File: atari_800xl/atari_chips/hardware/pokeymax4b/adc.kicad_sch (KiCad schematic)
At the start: 5 parts

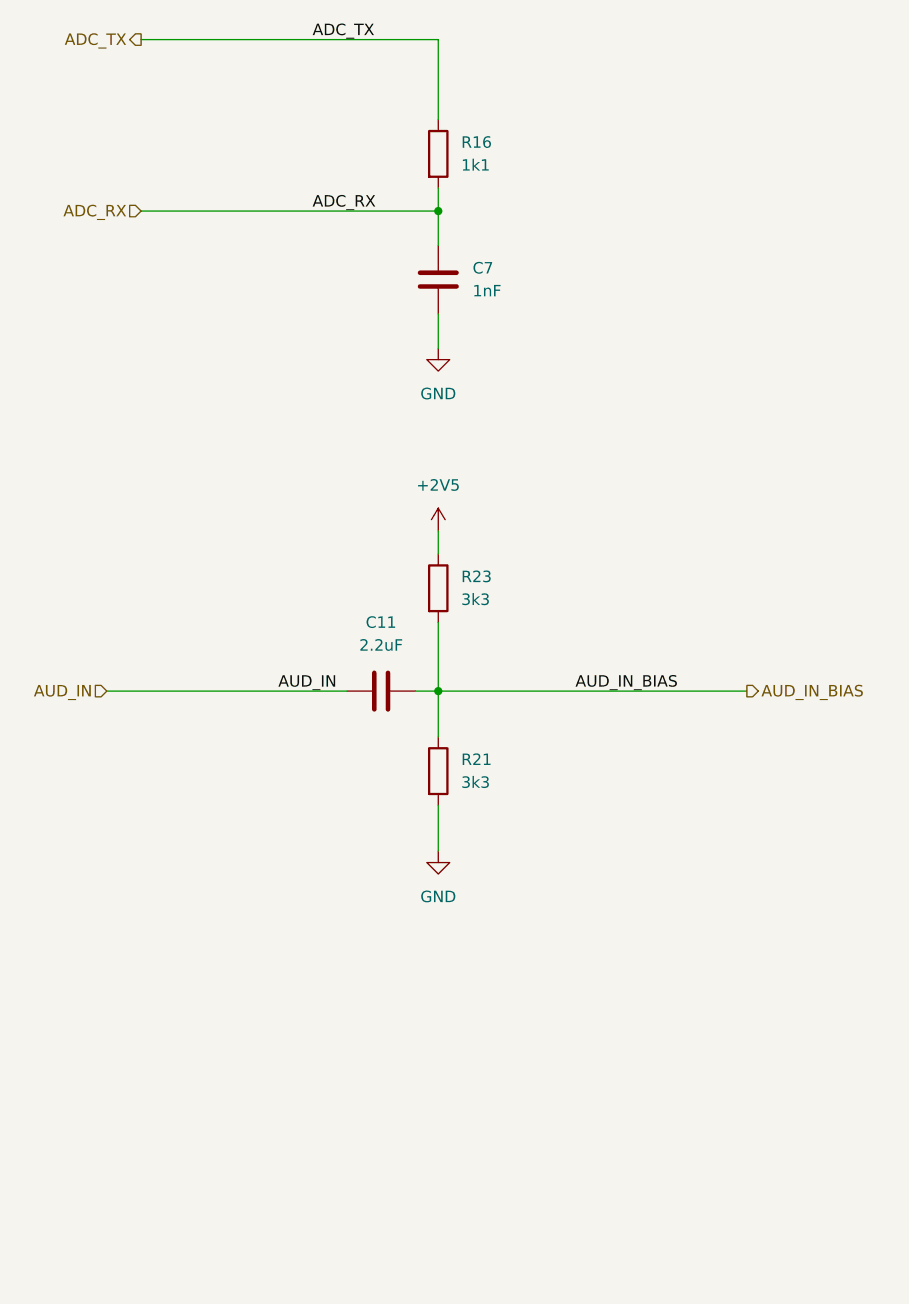
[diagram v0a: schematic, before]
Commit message: After testing 4b first run, there are a few issues. Updated to 4b2 with: Corrected L/R output. ADC bias improvement. ADC preamp out/in- corrected. Moved silkscreen name!
git-svn-id: svn+ssh://192.168.0.3/home/svnfpga/repo/trunk@1475 d6161ac3-aae1-4d52-9b05-ea9ac36b53d3
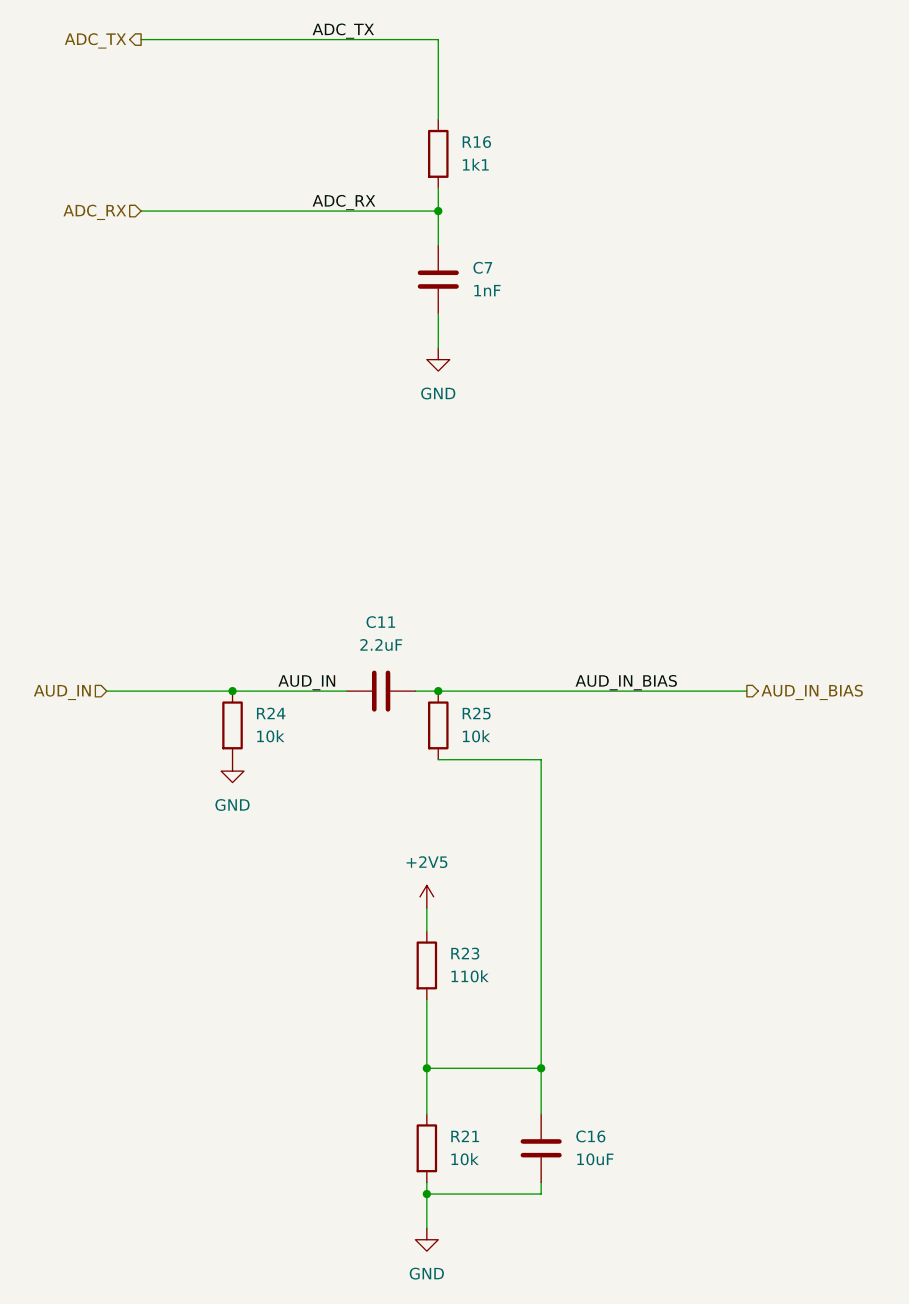
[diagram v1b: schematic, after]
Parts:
- added C16: 10uF, Capacitor_SMD:C_0603_1608Metric, symbol Device:C
- added R24, R25: 10k, Resistor_SMD:R_0603_1608Metric, symbol Device:R
- R21: value 3k3 -> 10k
- R23: value 3k3 -> 110k
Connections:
- net AUD_IN: now also R24.1
- net AUD_IN_BIAS: now also R25.1; no longer R21.1, R23.2
- net GND: now also C16.1, R24.2
- new net: C16.2, R21.1, R23.2, R25.2
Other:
- moved on the sheet: R21, R23
